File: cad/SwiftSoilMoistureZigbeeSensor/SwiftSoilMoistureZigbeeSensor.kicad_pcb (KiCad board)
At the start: 2 copper layers, 80 x 22.9 mm, 13 parts, among them J1 Probe, J3 ARM SWD, Q1 BSS84, SW1 Factory Reset, U1 TPS61221DCK, U2 E73-2G4M08S1C

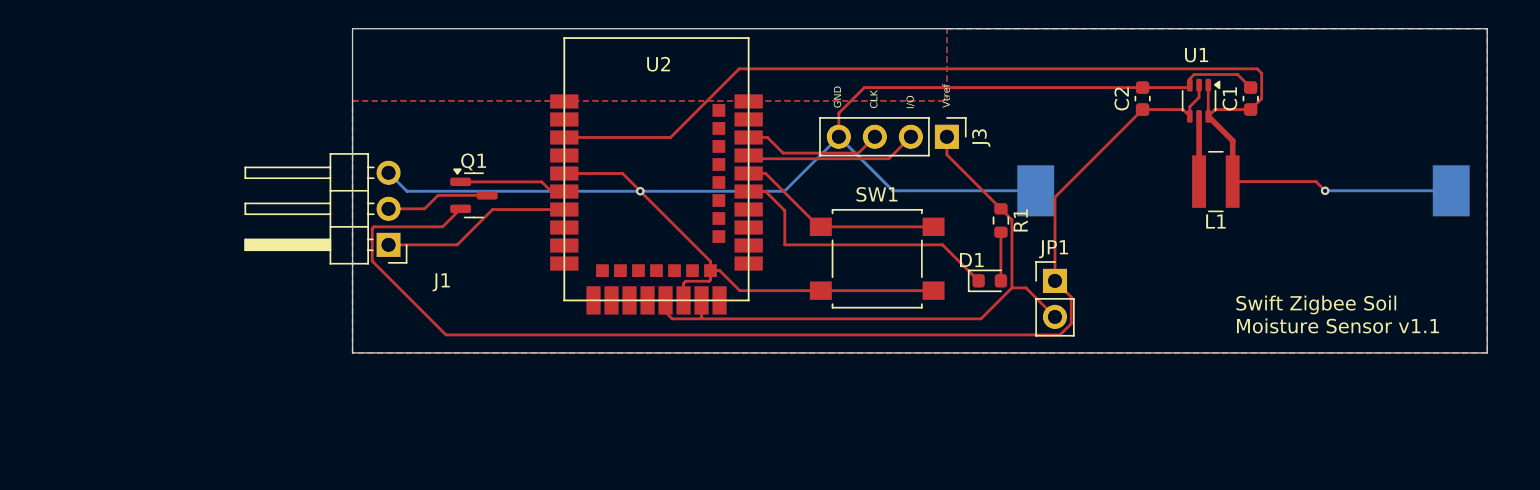
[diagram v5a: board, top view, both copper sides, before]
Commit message: Inductance footprint modified. Probe print
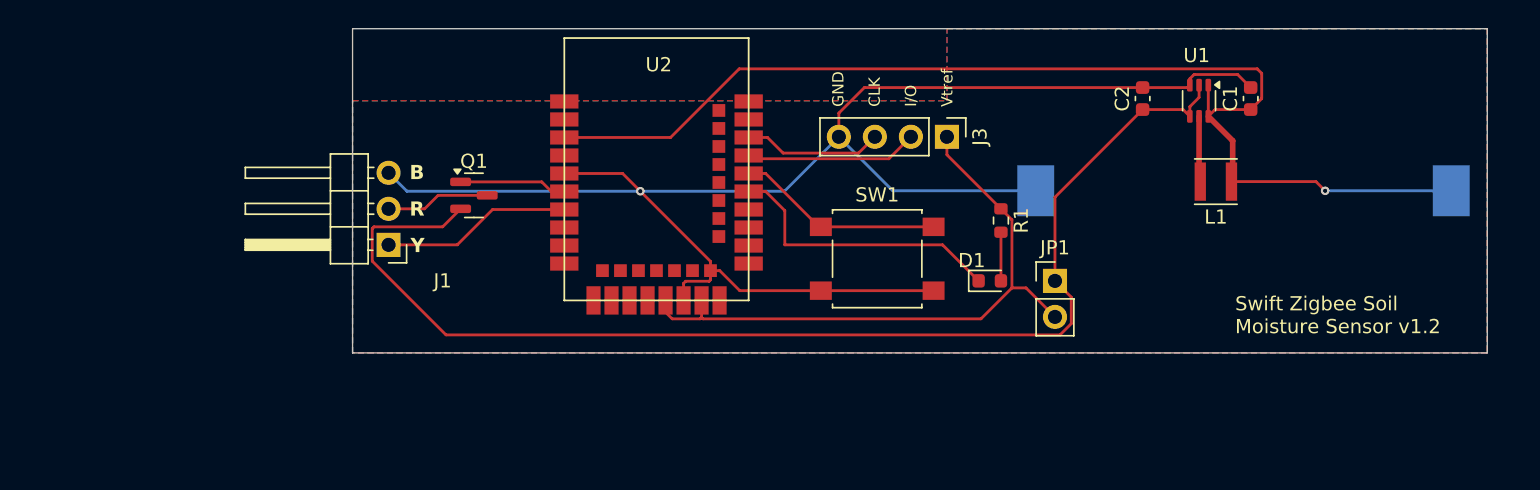
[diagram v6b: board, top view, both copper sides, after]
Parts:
- L1: footprint Inductor_SMD:L_Wuerth_MAPI-4020 -> Inductor_SMD:L_Taiyo-Yuden_NR-30xx
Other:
- board text added: "B"
- board text added: "R"
- board text added: "Swift Zigbee Soil Moisture Sensor v1.2"
- board text added: "Y"
- board text removed: "Swift Zigbee Soil Moisture Sensor v1.1"
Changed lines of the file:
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@@
   (title_block
     (title "Swift Zigbee Soil Moisture Sensor")
-    (date "2024-08-26")
-    (rev "1.1")
+    (date "2024-09-17")
+    (rev "1.2")
   )
   (layers
@@
     )
   )
-  (footprint "Inductor_SMD:L_Wuerth_MAPI-4020" (layer "F.Cu")
+  (footprint "Inductor_SMD:L_Taiyo-Yuden_NR-30xx" (layer "F.Cu")
     (at 139.615 53.96 180)
-    (descr "Inductor, Wuerth Elektronik, Wuerth_MAPI-4020, 4.0mmx4.0mm")
-    (tags "inductor Wuerth smd")
+    (descr "Inductor, Taiyo Yuden, NR series, Taiyo-Yuden_NR-30xx, 3.0mmx3.0mm")
+    (tags "inductor taiyo-yuden nr smd")
     (property "LCSC" "C87172")
     (property "Sheetfile" "SwiftSoilMoistureZigbeeSensor.kicad_sch")
@@
     (property "ki_keywords" "inductor choke coil reactor magnetic")
     (attr smd)
-    (fp_text reference "L1" (at 0 -2.85) (layer "F.SilkS")
-        (effects (font (size 1 1) (thickness 0.15)))
-    )
-    (fp_text value "4.7µH" (at 0 3.35) (layer "F.Fab") hide
-        (effects (font (size 1 1) (thickness 0.15)))
-    )
-    (fp_line (start -0.495 -2.1) (end 0.495 -2.1)
-      (stroke (width 0.12) (type solid)) (layer "F.SilkS"))
-    (fp_line (start -0.495 2.1) (end 0.495 2.1)
-      (stroke (width 0.12) (type solid)) (layer "F.SilkS"))
-    (fp_line (start -2 -2.2) (end -2 2.2)
-      (stroke (width 0.05) (type solid)) (layer "F.CrtYd"))
-    (fp_line (start -2 2.2) (end 2 2.2)
-      (stroke (width 0.05) (type solid)) (layer "F.CrtYd"))
-    (fp_line (start 2 -2.2) (end -2 -2.2)
-      (stroke (width 0.05) (type solid)) (layer "F.CrtYd"))
-    (fp_line (start 2 2.2) (end 2 -2.2)
-      (stroke (width 0.05) (type solid)) (layer "F.CrtYd"))
-    (fp_line (start -2 -2) (end -2 2)
-      (stroke (width 0.1) (type solid)) (layer "F.Fab"))
-    (fp_line (start -2 2) (end 2 2)
-      (stroke (width 0.1) (type solid)) (layer "F.Fab"))
-    (fp_line (start 2 -2) (end -2 -2)
-      (stroke (width 0.1) (type solid)) (layer "F.Fab"))
-    (fp_line (start 2 2) (end 2 -2)
-      (stroke (width 0.1) (type solid)) (layer "F.Fab"))
-    (pad "1" smd rect (at -1.185 0 180) (size 0.98 3.7) (layers "F.Cu" "F.Paste" "F.Mask")
+    (fp_text reference "L1" (at 0 -2.5 180) (layer "F.SilkS")
+        (effects (font (size 1 1) (thickness 0.15)))
+    )
+    (fp_text value "4.7µH" (at 0 3 180) (layer "F.Fab")
+        (effects (font (size 1 1) (thickness 0.15)))
+    )
+    (fp_text user "${REFERENCE}" (at 0 0 180) (layer "F.Fab")
+        (effects (font (size 0.7 0.7) (thickness 0.105)))
+    )
+    (fp_line (start -1.5 -1.6) (end 1.5 -1.6)
+      (stroke (width 0.12) (type solid)) (layer "F.SilkS"))
+    (fp_line (start -1.5 1.6) (end 1.5 1.6)
+      (stroke (width 0.12) (type solid)) (layer "F.SilkS"))
+    (fp_line (start -1.8 -1.8) (end -1.8 1.8)
+      (stroke (width 0.05) (type solid)) (layer "F.CrtYd"))
+    (fp_line (start -1.8 1.8) (end 1.8 1.8)
+      (stroke (width 0.05) (type solid)) (layer "F.CrtYd"))
+    (fp_line (start 1.8 -1.8) (end -1.8 -1.8)
+      (stroke (width 0.05) (type solid)) (layer "F.CrtYd"))
+    (fp_line (start 1.8 1.8) (end 1.8 -1.8)
+      (stroke (width 0.05) (type solid)) (layer "F.CrtYd"))
+    (fp_line (start -1.5 -0.95) (end -1.5 0.95)
+      (stroke (width 0.1) (type solid)) (layer "F.Fab"))
+    (fp_line (start -1.5 -0.95) (end -0.95 -1.5)
+      (stroke (width 0.1) (type solid)) (layer "F.Fab"))
+    (fp_line (start -1.5 0.95) (end -0.95 1.5)
+      (stroke (width 0.1) (type solid)) (layer "F.Fab"))
+    (fp_line (start -0.95 -1.5) (end 0.95 -1.5)
+      (stroke (width 0.1) (type solid)) (layer "F.Fab"))
+    (fp_line (start -0.95 1.5) (end 0.95 1.5)
+      (stroke (width 0.1) (type solid)) (layer "F.Fab"))
+    (fp_line (start 1.5 -0.95) (end 0.95 -1.5)
+      (stroke (width 0.1) (type solid)) (layer "F.Fab"))
+    (fp_line (start 1.5 0.95) (end 0.95 1.5)
+      (stroke (width 0.1) (type solid)) (layer "F.Fab"))
+    (fp_line (start 1.5 0.95) (end 1.5 -0.95)
+      (stroke (width 0.1) (type solid)) (layer "F.Fab"))
+    (pad "1" smd rect (at -1.1 0 180) (size 0.8 2.7) (layers "F.Cu" "F.Paste" "F.Mask")
       (net 1 "Net-(BT1-+)") (pinfunction "1") (pintype "passive"))
-    (pad "2" smd rect (at 1.185 0 180) (size 0.98 3.7) (layers "F.Cu" "F.Paste" "F.Mask")
+    (pad "2" smd rect (at 1.1 0 180) (size 0.8 2.7) (layers "F.Cu" "F.Paste" "F.Mask")
       (net 7 "Net-(U1-L)") (pinfunction "2") (pintype "passive"))
-    (model "${KICAD6_3DMODEL_DIR}/Inductor_SMD.3dshapes/L_Wuerth_MAPI-4020.wrl"
+    (model "${KICAD6_3DMODEL_DIR}/Inductor_SMD.3dshapes/L_Taiyo-Yuden_NR-30xx.wrl"
       (offset (xyz 0 0 0))
       (scale (xyz 1 1 1))
@@
   (gr_rect (start 78.74 43.18) (end 158.75 66.04)
     (stroke (width 0.05) (type default)) (fill none) (layer "Edge.Cuts"))
-  (gr_text "GND" (at 113.244234 48.784336 90) (layer "F.SilkS")
-    (effects (font (size 0.5 0.5) (thickness 0.1)) (justify left bottom))
-  )
-  (gr_text "I/O" (at 118.365243 48.848497 90) (layer "F.SilkS")
-    (effects (font (size 0.5 0.5) (thickness 0.1)) (justify left bottom))
-  )
-  (gr_text "CLK" (at 115.803547 48.81388 90) (layer "F.SilkS")
-    (effects (font (size 0.5 0.5) (thickness 0.1)) (justify left bottom))
-  )
-  (gr_text "Swift Zigbee Soil\nMoisture Sensor v1.1" (at 140.97 64.77) (layer "F.SilkS")
+  (gr_text "B" (at 82.754745 53.90597) (layer "F.SilkS")
+    (effects (font (size 1 1) (thickness 0.2) bold) (justify left bottom))
+  )
+  (gr_text "GND" (at 113.453944 48.692718 90) (layer "F.SilkS")
+    (effects (font (size 0.8 0.8) (thickness 0.1)) (justify left bottom))
+  )
+  (gr_text "Y" (at 82.826174 59.05041) (layer "F.SilkS")
+    (effects (font (size 1 1) (thickness 0.2) bold) (justify left bottom))
+  )
+  (gr_text "R" (at 82.754745 56.47819) (layer "F.SilkS")
+    (effects (font (size 1 1) (thickness 0.2) bold) (justify left bottom))
+  )
+  (gr_text "I/O" (at 118.577336 48.692718 90) (layer "F.SilkS")
+    (effects (font (size 0.8 0.8) (thickness 0.1)) (justify left bottom))
+  )
+  (gr_text "CLK" (at 116.01564 48.692718 90) (layer "F.SilkS")
+    (effects (font (size 0.8 0.8) (thickness 0.1)) (justify left bottom))
+  )
+  (gr_text "Swift Zigbee Soil\nMoisture Sensor v1.2" (at 140.97 64.77) (layer "F.SilkS")
     (effects (font (size 1 1) (thickness 0.1)) (justify left bottom))
   )
-  (gr_text "Vtref" (at 120.909631 48.761953 90) (layer "F.SilkS")
-    (effects (font (size 0.5 0.5) (thickness 0.1)) (justify left bottom))
+  (gr_text "Vtref" (at 121.139032 48.692718 90) (layer "F.SilkS")
+    (effects (font (size 0.8 0.8) (thickness 0.1)) (justify left bottom))
   )
   (segment (start 142.845 46.325) (end 142.845 48.105) (width 0.2) (layer "F.Cu") (net 1))
